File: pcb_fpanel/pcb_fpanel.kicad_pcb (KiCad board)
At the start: 2 copper layers, 61 x 160 mm, 40 parts, among them J1 Conn_01x18, J2 Conn_01x04, J3 Conn_01x10, SW1 Rotary_Encoder_Switch, SW10 SW_Push_LED, SW13 SW_Push_LED, SW14 SW_Push_LED, SW17 SW_Push_LED, SW18 SW_Push_LED, SW20 SW_Push_LED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

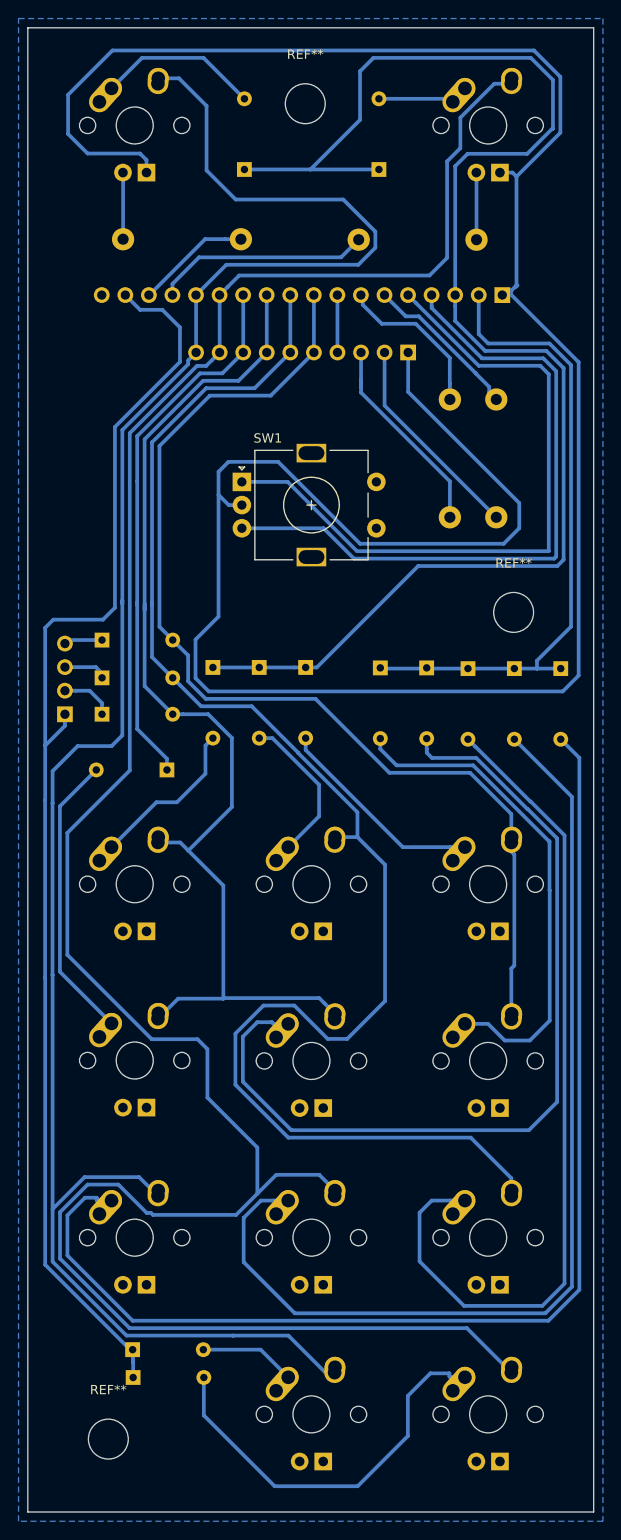
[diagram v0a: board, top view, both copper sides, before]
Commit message: Frontpanel pcb korjaus: led-napit käännetty ja yhteensopivuus arduino pro micron kanssa
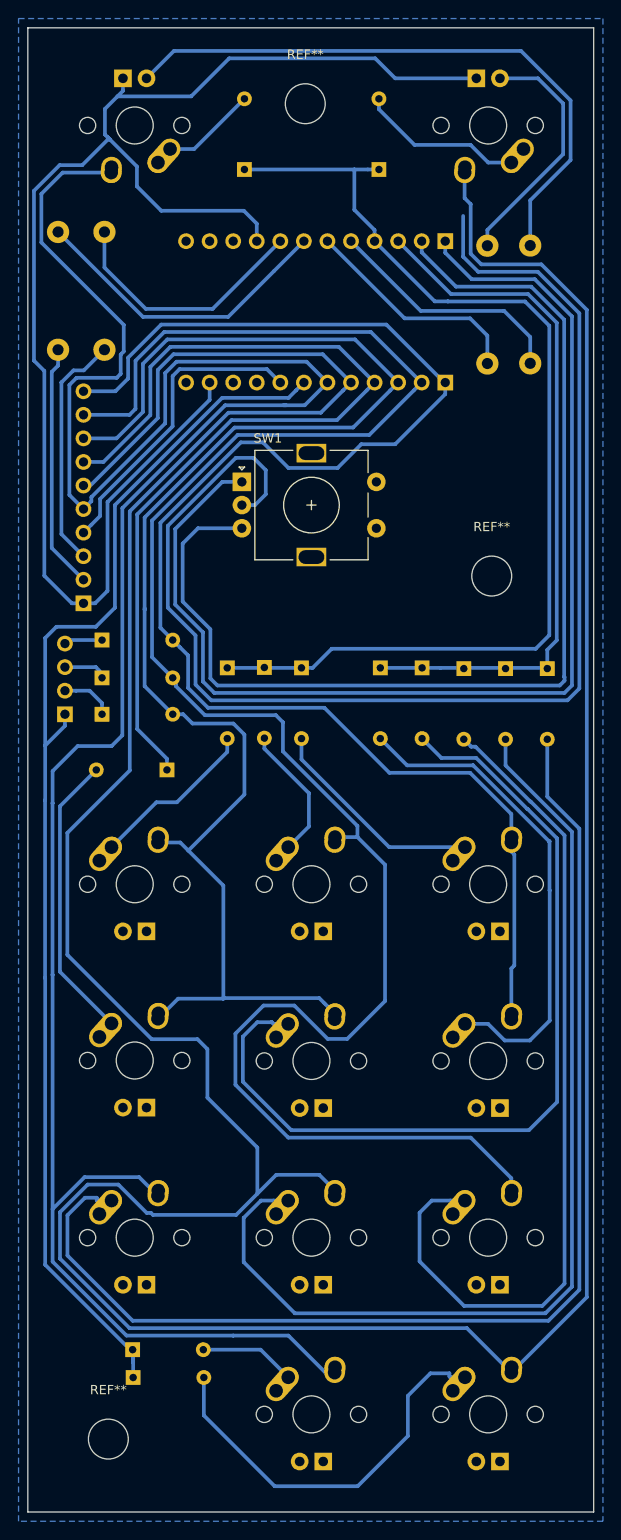
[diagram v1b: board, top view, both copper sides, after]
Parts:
- added J4: Conn_01x12, Pin_Headers:Pin_Header_Straight_1x12_Pitch2.54mm, B.Cu at (94.0, 56.2)
- J1: value Conn_01x18 -> Conn_01x12; footprint Pin_Headers:Pin_Header_Straight_1x18_Pitch2.54mm -> Pin_Headers:Pin_Header_Straight_1x12_Pitch2.54mm
- moved R1 45.9 mm to (57.3, 52.7)
- moved R2 45.9 mm to (52.3, 52.7)
- moved J3 44.2 mm to (55.0, 80.0), turned to 0 degrees
- moved R4 39.3 mm to (98.5, 41.5), turned to 270 degrees
- moved J1 8.46 mm to (94.0, 41.0)
- moved R3 5.82 mm to (103.2, 41.5), turned to 270 degrees
- moved REF** 4.58 mm to (99.0, 77.1)
- moved D21 1.55 mm to (70.5, 87.0)
- moved D1 1.45 mm to (105.0, 87.1)
- moved D9 0.95 mm to (100.5, 87.1)
- moved D14 0.55 mm to (74.5, 87.0)
- moved D22 0.50 mm to (91.5, 87.0)
- moved D17 0.45 mm to (78.5, 87.0)
- moved D13 0.45 mm to (96.0, 87.1)
- turned SW3 to 180 degrees
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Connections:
- J1 pad 1: GNDD -> Net-(J1-Pad1)
- J1 pad 10: column_3 -> Net-(J1-Pad10)
- J1 pad 11: column_5 -> Net-(J1-Pad11)
- J1 pad 12: row_2 -> Net-(J1-Pad12)
- J1 pad 2: row_4 -> Net-(J1-Pad2)
- J1 pad 3: row_3 -> row_4
- J1 pad 4: Net-(J1-Pad4) -> row_3
- J1 pad 8: row_1 -> Net-(J1-Pad8)
- J1 pad 9: column_4 -> GNDD
- J3 pad 10: column_1 -> column_4
- J3 pad 2: led_1 -> led_2
- J3 pad 3: led_2 -> led_1
- J3 pad 5: column_4 -> column_1
- J3 pad 6: column_3 -> column_2
- J3 pad 7: column_5 -> row_2
- J3 pad 8: row_2 -> column_5
- J3 pad 9: column_2 -> column_3
- R1 pad 2: Net-(J1-Pad6) -> Net-(J1-Pad8)
- R3 pad 2: Net-(J1-Pad15) -> Net-(J1-Pad5)
- R4 pad 2: Net-(J1-Pad16) -> Net-(J1-Pad6)
- SW1 pad A: Net-(J1-Pad5) -> Net-(J1-Pad1)
- SW1 pad B: Net-(J1-Pad4) -> Net-(J1-Pad2)
- SW3 pad 3: led_4 -> led_3
- SW8 pad 3: led_3 -> led_4
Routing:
- net column_2: track 258.0 -> 391.0 mm
- net Net-(J1-Pad1): track 0.00 -> 125.1 mm
- net Net-(J1-Pad2): track 0.00 -> 120.1 mm
- net Net-(J1-Pad4): track 73.0 -> 0.00 mm
- net led_4: track 7.24 -> 66.6 mm
- net column_4: track 117.4 -> 168.3 mm
- net column_3: track 163.6 -> 211.7 mm
- net Net-(J1-Pad5): track 74.0 -> 26.5 mm
- net column_5: track 118.2 -> 164.8 mm
- net row_3: track 160.9 -> 115.3 mm
- net row_2: track 58.9 -> 101.5 mm
- net column_1: track 219.9 -> 252.4 mm
- net Net-(J1-Pad8): track 0.00 -> 27.7 mm
- net row_1: track 6.19 -> 33.4 mm
- net GNDD: track 274.8 -> 300.4 mm
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
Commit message: Interrupt pinnit muutettu PC->Ext
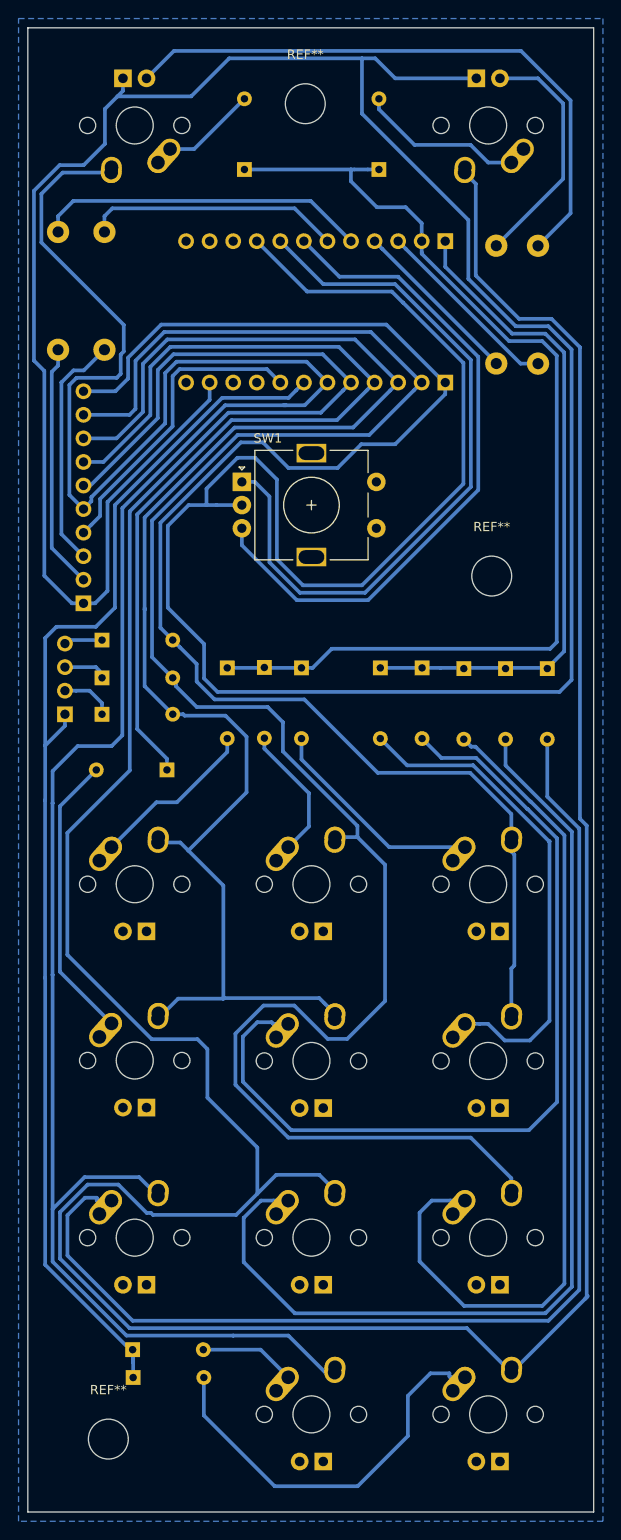
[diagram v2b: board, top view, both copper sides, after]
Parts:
- moved R4 0.96 mm to (99.5, 41.5)
- moved R3 0.84 mm to (104.0, 41.5)
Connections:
- J1 pad 1: Net-(J1-Pad1) -> row_4
- J1 pad 2: Net-(J1-Pad2) -> row_3
- J1 pad 3: row_4 -> Net-(J1-Pad3)
- J1 pad 4: row_3 -> Net-(J1-Pad4)
- R1 pad 2: Net-(J1-Pad8) -> Net-(J1-Pad6)
- R2 pad 2: Net-(J1-Pad7) -> Net-(J1-Pad5)
- R3 pad 2: Net-(J1-Pad5) -> Net-(J1-Pad3)
- R4 pad 2: Net-(J1-Pad6) -> Net-(J1-Pad4)
- SW1 pad A: Net-(J1-Pad1) -> Net-(J1-Pad8)
- SW1 pad B: Net-(J1-Pad2) -> Net-(J1-Pad7)
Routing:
- net Net-(J1-Pad1): track 125.1 -> 0.00 mm
- net Net-(J1-Pad2): track 120.1 -> 0.00 mm
- net GNDD: track 300.4 -> 369.5 mm
- net Net-(J1-Pad8): track 27.7 -> 78.0 mm
- net Net-(J1-Pad7): track 33.7 -> 73.0 mm
- net Net-(J1-Pad3): track 0.00 -> 20.5 mm
- net Net-(J1-Pad4): track 0.00 -> 18.6 mm
- net Net-(J1-Pad5): track 26.5 -> 35.8 mm
- net row_4: track 76.5 -> 72.3 mm
- net Net-(J1-Pad6): track 24.5 -> 27.6 mm
- net column_2: track 391.0 -> 389.7 mm
- net column_4: track 168.3 -> 167.4 mm

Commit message: Näppäinmatriisin srakkeille lisätty etuvastukset
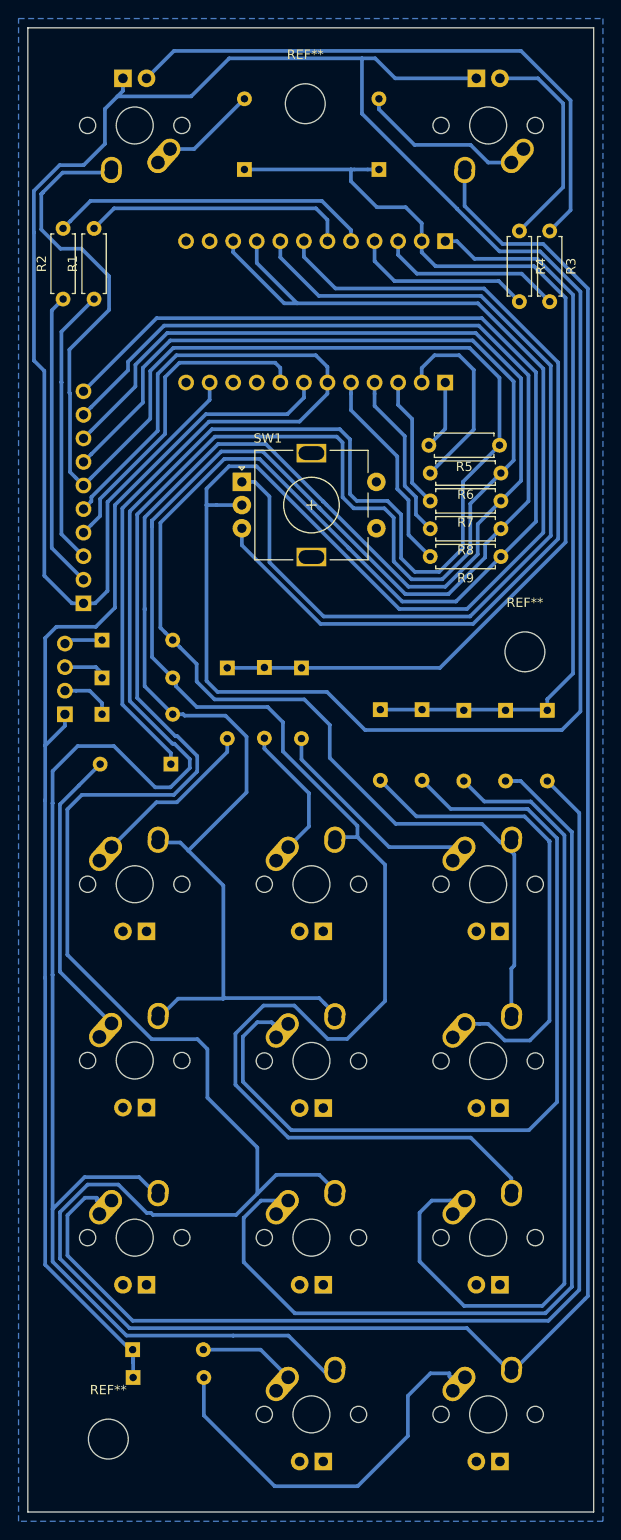
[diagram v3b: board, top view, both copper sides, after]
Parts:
- added R5: R, Resistors_THT:R_Axial_DIN0207_L6.3mm_D2.5mm_P7.62mm_Horizontal, F.Cu at (99.8, 63.0)
- added R6: R, Resistors_THT:R_Axial_DIN0207_L6.3mm_D2.5mm_P7.62mm_Horizontal, F.Cu at (100.0, 66.0)
- added R7: R, Resistors_THT:R_Axial_DIN0207_L6.3mm_D2.5mm_P7.62mm_Horizontal, F.Cu at (100.0, 69.0)
- added R8: R, Resistors_THT:R_Axial_DIN0207_L6.3mm_D2.5mm_P7.62mm_Horizontal, F.Cu at (100.0, 72.0)
- added R9: R, Resistors_THT:R_Axial_DIN0207_L6.3mm_D2.5mm_P7.62mm_Horizontal, F.Cu at (100.0, 75.0)
- R1, R2, R3, R4: footprint Resistors_THT:R_Axial_DIN0411_L9.9mm_D3.6mm_P12.70mm_Horizontal -> Resistors_THT:R_Axial_DIN0207_L6.3mm_D2.5mm_P7.62mm_Horizontal; moved to F.Cu
- moved REF** 8.92 mm to (102.6, 85.3)
- moved R1 5.58 mm to (56.1, 47.2)
- moved R2 5.49 mm to (52.8, 47.2)
- moved D1 4.50 mm to (105.0, 91.6)
- moved D13 4.50 mm to (96.0, 91.6)
- moved D18 4.50 mm to (87.0, 91.5)
- moved D22 4.50 mm to (91.5, 91.5)
- moved D9 4.50 mm to (100.5, 91.6)
- moved R4 2.95 mm to (102.0, 39.9)
- moved R3 2.04 mm to (105.3, 39.9)
- moved D20 0.75 mm to (64.4, 97.4)
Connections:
- J1 pad 10: Net-(J1-Pad10) -> GNDD
- J3 pad 5: column_1 -> row_2
- J3 pad 6: column_2 -> column_1
- J3 pad 7: row_2 -> column_2
- J4 pad 1: column_4 -> Net-(J4-Pad1)
- J4 pad 2: column_3 -> Net-(J4-Pad2)
- J4 pad 3: column_5 -> Net-(J4-Pad3)
- J4 pad 4: row_2 -> Net-(J4-Pad4)
- J4 pad 5: column_2 -> Net-(J4-Pad5)
- J4 pad 6: column_1 -> row_2
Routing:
- net column_1: track 252.4 -> 326.6 mm
- net column_2: track 389.7 -> 462.6 mm
- net column_5: track 165.0 -> 211.7 mm
- net column_3: track 211.7 -> 255.2 mm
- net column_4: track 167.4 -> 205.9 mm
- net GNDD: track 369.5 -> 400.2 mm
- net Net-(J1-Pad8): track 78.0 -> 101.1 mm
- net Net-(J1-Pad7): track 73.0 -> 96.1 mm
- net Net-(J4-Pad5): track 0.00 -> 22.3 mm
- net Net-(J4-Pad2): track 0.00 -> 21.5 mm
- net Net-(J4-Pad4): track 0.00 -> 18.2 mm
- net Net-(J4-Pad3): track 0.00 -> 14.2 mm
- net row_4: track 72.3 -> 80.1 mm
- net Net-(J4-Pad1): track 0.00 -> 7.49 mm
- net led_2: track 26.5 -> 32.2 mm
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
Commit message: Reikien siirtelyä
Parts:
- J2: value Conn_01x04 -> Conn_01x03; footprint Pin_Headers:Pin_Header_Straight_1x04_Pitch2.54mm -> Pin_Headers:Pin_Header_Straight_1x03_Pitch2.54mm; moved to F.Cu
- moved D6 30.2 mm to (86.6, 78.0), turned to 270 degrees
- moved REF** 2.94 mm to (57.0, 173.0)
- moved REF** 1.22 mm to (103.8, 85.4)
- turned J2 to 180 degrees
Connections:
- D6 pad 1: Net-(D6-Pad1) -> encoder_button
- SW1 pad S1: Net-(SW1-PadS1) -> encoder_button
- SW1 pad S2: Net-(SW1-PadS2) -> row_5
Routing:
- net row_5: track 136.1 -> 162.3 mm, vias 0 -> 2
- net GNDD: track 400.2 -> 413.0 mm
- net column_4: track 205.9 -> 218.5 mm
- net column_5: track 211.7 -> 220.1 mm
- net Net-(J1-Pad8): track 101.1 -> 109.5 mm
- net Net-(J1-Pad7): track 96.1 -> 104.3 mm
- net column_3: track 255.2 -> 263.3 mm
- net encoder_button: track 0.00 -> 6.06 mm
- net row_4: track 80.1 -> 84.8 mm
- net Net-(D6-Pad1): track 4.16 -> 0.00 mm
- net row_3: track 114.4 -> 116.7 mm
- net column_1: track 326.6 -> 325.8 mm
- net Net-(D21-Pad2): track 18.2 -> 18.7 mm
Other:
- net class Default: via_dia 0.8 -> 2; via_drill 0.4 -> 1

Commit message: Näppäinten sijainnit ja footprintit päivitetty
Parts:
- SW10, SW13, SW14, SW17, SW18, SW20, SW21, SW22, SW3, SW4, SW5, SW8, SW9: footprint MX_Alps_Hybrid:MX-1U -> MX_Only:MXOnly-1U
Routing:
- net Net-(D10-Pad2): track 43.4 -> 40.0 mm
- net Net-(D1-Pad2): track 125.9 -> 122.6 mm
- net Net-(D9-Pad2): track 107.7 -> 104.9 mm
- net Net-(D13-Pad2): track 90.9 -> 88.5 mm
- net Net-(D14-Pad2): track 14.7 -> 16.7 mm
- net Net-(D21-Pad2): track 18.7 -> 20.7 mm
- net Net-(D4-Pad2): track 17.8 -> 19.7 mm
- net Net-(D18-Pad2): track 51.1 -> 53.0 mm
- net column_5: track 220.1 -> 221.6 mm
- net Net-(D20-Pad2): track 32.0 -> 33.0 mm
- net Net-(D17-Pad2): track 23.8 -> 23.1 mm
- net Net-(D5-Pad2): track 10.4 -> 9.68 mm

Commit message: pcb_fpanel: Käyttämättömien ledien reiät poistettu
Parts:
- SW10, SW13, SW14, SW17, SW18, SW20, SW21, SW22, SW4, SW5, SW9: footprint MX_Only:MXOnly-1U -> MX_Only:MXOnly-1U-NoLED
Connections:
- SW3 pad 3: led_3 -> (no net)
- SW3 pad 4: GNDD -> (no net)
- SW8 pad 3: led_4 -> (no net)
- SW8 pad 4: GNDD -> (no net)

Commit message: pcb_fpanel: Kytkimien footprintien reikätyyppejä muutettu
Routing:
- added copper zone on B.Cu, net (none)
